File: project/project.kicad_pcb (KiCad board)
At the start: 4 copper layers, 84 x 84 mm, 163 parts, among them J101 BUS, J102 BUS, J103 FFC, J104 Back, J105 Front, J301 5V, J302 24V, J303 3V3, J401 USB_C_Receptacle_USB2.0, SW101 SW_DIP_x04, SW401 RST, SW402 MOD, U101 GX101, U102 GX101, U201 74HC595, U202 ULN2803A, U203 74HC595, U204 ULN2803A, U301 ME3121AM6G, U302 MT3406, U401 esp32-C3FH4X, U402 XL1050, U403 USBLC6-2SC6, Y401 40MHz

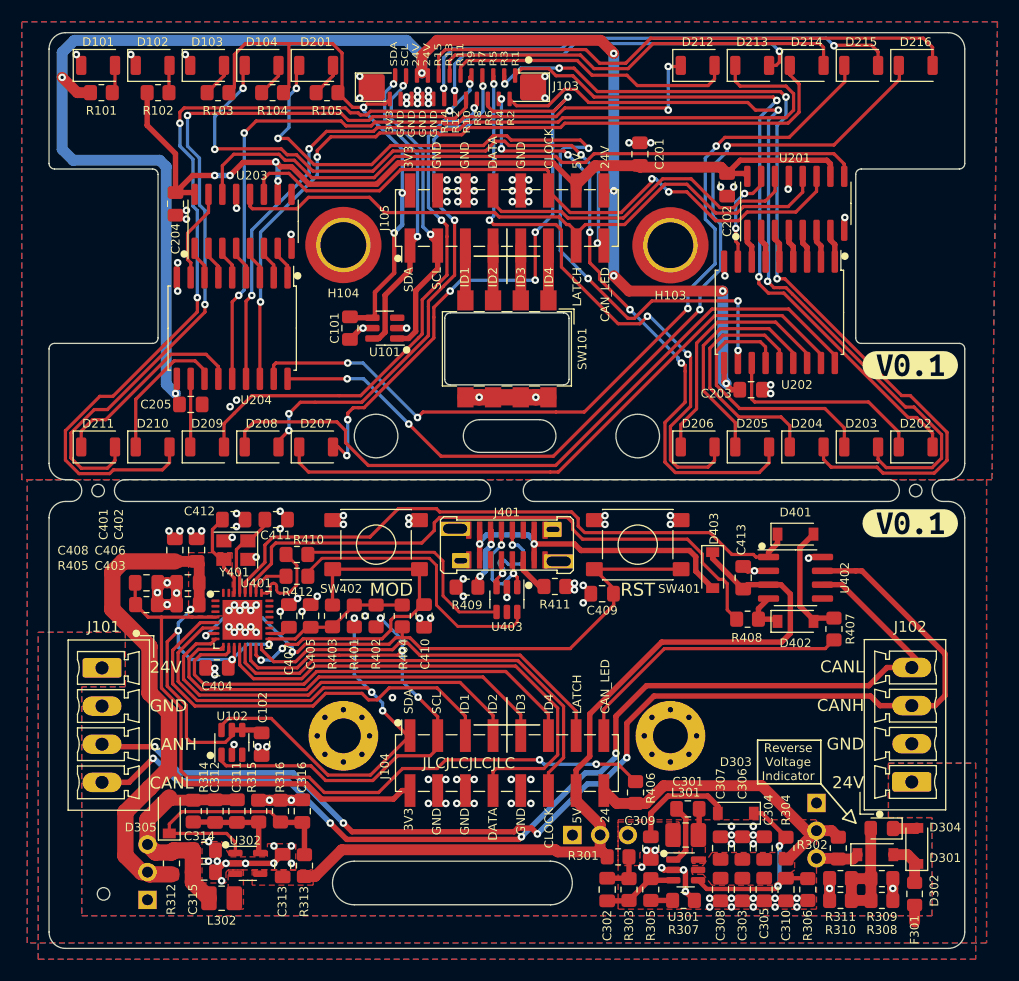
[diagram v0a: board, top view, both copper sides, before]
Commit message: adjusting hole sizes and adding qfn model
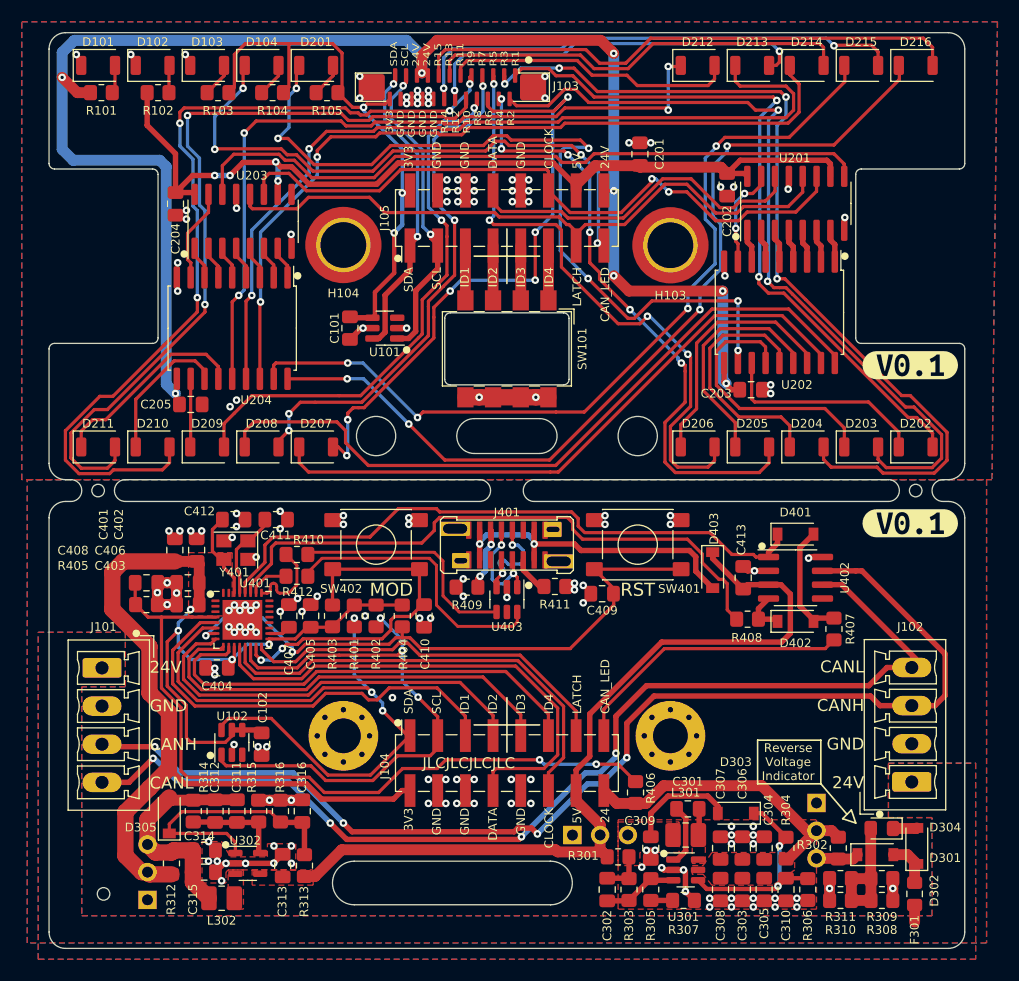
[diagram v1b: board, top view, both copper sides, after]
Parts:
- U401: footprint Package_DFN_QFN:QFN-32-1EP_5x5mm_P0.5mm_EP3.65x3.65mm -> -local:QFN-32-1EP_5x5mm_P0.5mm_EP3.65x3.65mm
- moved kibuzzard-6761E03A 0.20 mm to (168.3, 104.3)
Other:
- outline, holes or cut-outs redrawn

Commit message: few fixes and bumping up version
* reordering id bits
* moving silkscreen around
* adding hole in the center tab
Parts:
- removed kibuzzard-66DA8205: G***, kibuzzard-66DA8205
- removed kibuzzard-6750110D: G***, kibuzzard-6750110D
- removed kibuzzard-6752E14C: G***, kibuzzard-6752E14C
- removed kibuzzard-6752E284: G***, kibuzzard-6752E284
- removed kibuzzard-6752E2AC: G***, kibuzzard-6752E2AC
- removed kibuzzard-6752E2BE: G***, kibuzzard-6752E2BE
- removed kibuzzard-6752E2D3: G***, kibuzzard-6752E2D3
- removed kibuzzard-6752E2E5: G***, kibuzzard-6752E2E5
- removed kibuzzard-6752E328: G***, kibuzzard-6752E328
- removed kibuzzard-6752E335: G***, kibuzzard-6752E335
- removed kibuzzard-6752E395: G***, kibuzzard-6752E395
- removed kibuzzard-6752E39B: G***, kibuzzard-6752E39B
- removed kibuzzard-6752E3A1: G***, kibuzzard-6752E3A1
- removed kibuzzard-6752E3EF: G***, kibuzzard-6752E3EF
- removed kibuzzard-6752E3F8: G***, kibuzzard-6752E3F8
- removed kibuzzard-6752E3FE: G***, kibuzzard-6752E3FE
- removed kibuzzard-6752E405: G***, kibuzzard-6752E405
- removed kibuzzard-6752E427: G***, kibuzzard-6752E427
- removed kibuzzard-6752E433: G***, kibuzzard-6752E433
- removed kibuzzard-6752E441: G***, kibuzzard-6752E441
- removed kibuzzard-6752E448: G***, kibuzzard-6752E448
- removed kibuzzard-6752E44F: G***, kibuzzard-6752E44F
- removed kibuzzard-67570608: G***, kibuzzard-67570608
- removed kibuzzard-67570794: G***, kibuzzard-67570794
- removed kibuzzard-6757079A: G***, kibuzzard-6757079A
- removed kibuzzard-6761E03A: G***, kibuzzard-6761E03A
- removed kibuzzard-6761E048: G***, kibuzzard-6761E048
- removed kibuzzard-6761E1E4 (x2): G***, kibuzzard-6761E1E4
- added REF**: toolhole, -local:toolhole, F.Cu at (168.3, 112.5)
- added kibuzzard-679933C7: G***, kibuzzard-679933C7, F.Cu at (205.3, 101.0)
- added kibuzzard-679933D9: G***, kibuzzard-679933D9, F.Cu at (205.3, 115.5)
- added kibuzzard-67993413: G***, kibuzzard-67993413, B.Cu at (135.8, 106.5)
- added kibuzzard-67993427: G***, kibuzzard-67993427, B.Cu at (130.8, 107.0)
- added kibuzzard-67993436: G***, kibuzzard-67993436, B.Cu at (140.8, 106.5)
- added kibuzzard-67993449: G***, kibuzzard-67993449, B.Cu at (145.8, 106.5)
- added kibuzzard-67993459: G***, kibuzzard-67993459, B.Cu at (150.8, 106.5)
- added kibuzzard-679934A0: G***, kibuzzard-679934A0, B.Cu at (156.3, 104.0)
- added kibuzzard-679934B0: G***, kibuzzard-679934B0, B.Cu at (180.3, 104.0)
- added kibuzzard-679934DC: G***, kibuzzard-679934DC, B.Cu at (185.8, 106.5)
- added kibuzzard-679934EA: G***, kibuzzard-679934EA, B.Cu at (190.8, 106.5)
- added kibuzzard-67993507: G***, kibuzzard-67993507, B.Cu at (205.8, 106.5)
- added kibuzzard-67993514: G***, kibuzzard-67993514, B.Cu at (200.8, 106.5)
- added kibuzzard-67993518: G***, kibuzzard-67993518, B.Cu at (195.8, 106.5)
- added kibuzzard-6799352B: G***, kibuzzard-6799352B, B.Cu at (130.8, 75.0)
- added kibuzzard-67993537: G***, kibuzzard-67993537, B.Cu at (135.8, 75.5)
- added kibuzzard-67993543: G***, kibuzzard-67993543, B.Cu at (140.8, 75.0)
- added kibuzzard-67993570: G***, kibuzzard-67993570, B.Cu at (145.8, 75.0)
- added kibuzzard-6799357E: G***, kibuzzard-6799357E, B.Cu at (150.8, 75.0)
- added kibuzzard-67993590: G***, kibuzzard-67993590, B.Cu at (185.8, 75.0)
- added kibuzzard-6799359C: G***, kibuzzard-6799359C, B.Cu at (190.8, 75.0)
- added kibuzzard-679935A9: G***, kibuzzard-679935A9, B.Cu at (195.8, 75.0)
- added kibuzzard-679935B4: G***, kibuzzard-679935B4, B.Cu at (200.8, 75.0)
- added kibuzzard-679935C1: G***, kibuzzard-679935C1, B.Cu at (205.8, 75.0)
- added kibuzzard-679935E3: G***, kibuzzard-679935E3, B.Cu at (144.3, 151.0)
- added kibuzzard-679935F0: G***, kibuzzard-679935F0, B.Cu at (203.5, 152.2)
- added kibuzzard-6799365E: G***, kibuzzard-6799365E, B.Cu at (168.5, 122.8)
- added kibuzzard-67993A27: G***, kibuzzard-67993A27, B.Cu at (168.3, 104.4)
- moved G*** 3.61 mm to (168.5, 83.0)
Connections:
- J104 pad 11: B_ID4 -> B_ID1
- J104 pad 5: B_ID1 -> B_ID4
- J104 pad 7: B_ID2 -> B_ID3
- J104 pad 9: B_ID3 -> B_ID2
- J105 pad 11: F_ID4 -> F_ID1
- J105 pad 5: F_ID1 -> F_ID4
- J105 pad 7: F_ID2 -> F_ID3
- J105 pad 9: F_ID3 -> F_ID2
- SW101 pad 1: F_ID4 -> F_ID1
- SW101 pad 2: F_ID3 -> F_ID2
- SW101 pad 3: F_ID2 -> F_ID3
- SW101 pad 4: F_ID1 -> F_ID4
- U401 pad 10: B_ID4 -> B_ID1
- U401 pad 5: B_ID1 -> B_ID4
- U401 pad 8: B_ID2 -> B_ID3
- U401 pad 9: B_ID3 -> B_ID2
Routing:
- net B_ID4: track 42.2 -> 39.8 mm
- net B_ID1: track 39.8 -> 42.2 mm
- net B_ID3: track 40.0 -> 38.3 mm
- net B_ID2: track 38.3 -> 40.0 mm
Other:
- board text added: "SDA SCL ID4 ID3 ID2 ID1 LATCH CAN_LED"
- board text removed: "SDA SCL ID1 ID2 ID3 ID4 LATCH CAN_LED"

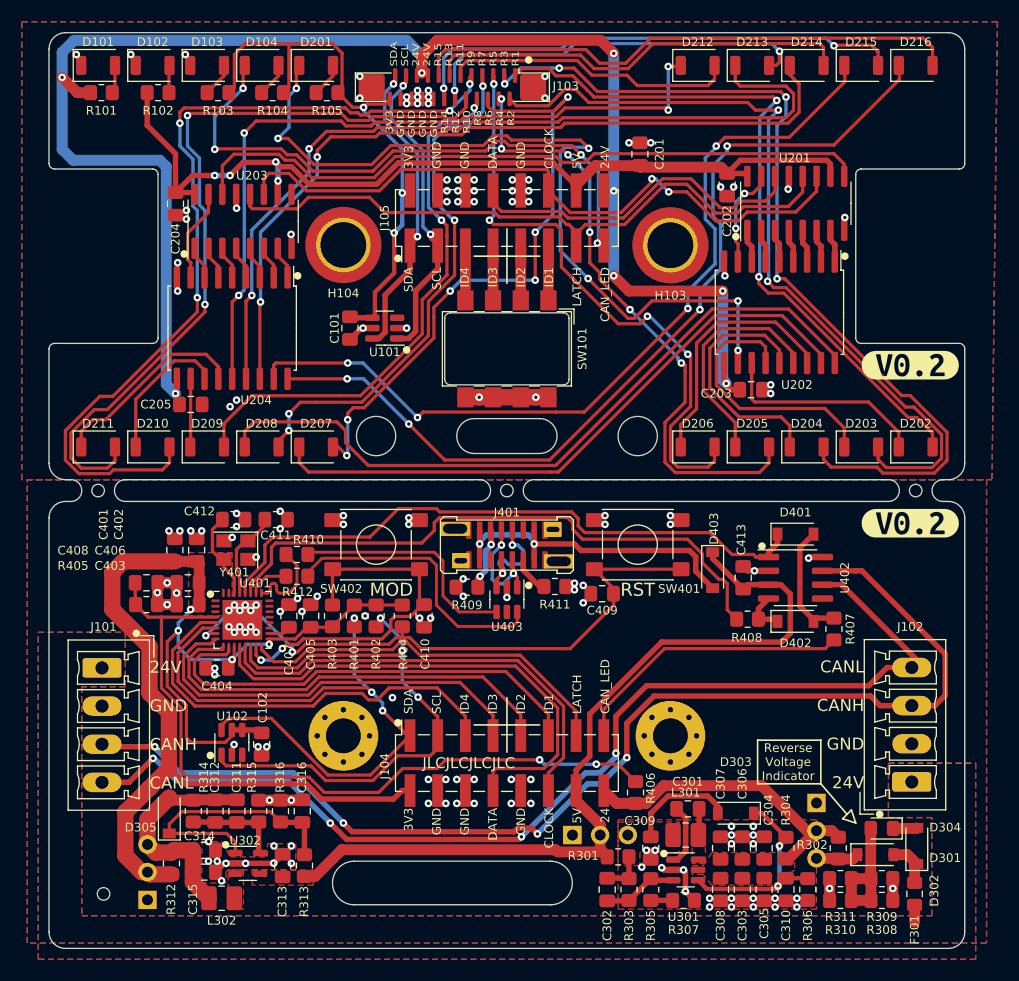
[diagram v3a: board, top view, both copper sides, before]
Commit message: improvements for next prototype
* buck makes 6v now
* using LDO for 5v with over voltage disable
* using LDO for 3v3
* adding zener to 24v led to stop it from glowing from 5v USB
* added 0.2mm heigt for USB port hole
* both buttons now 15mm height
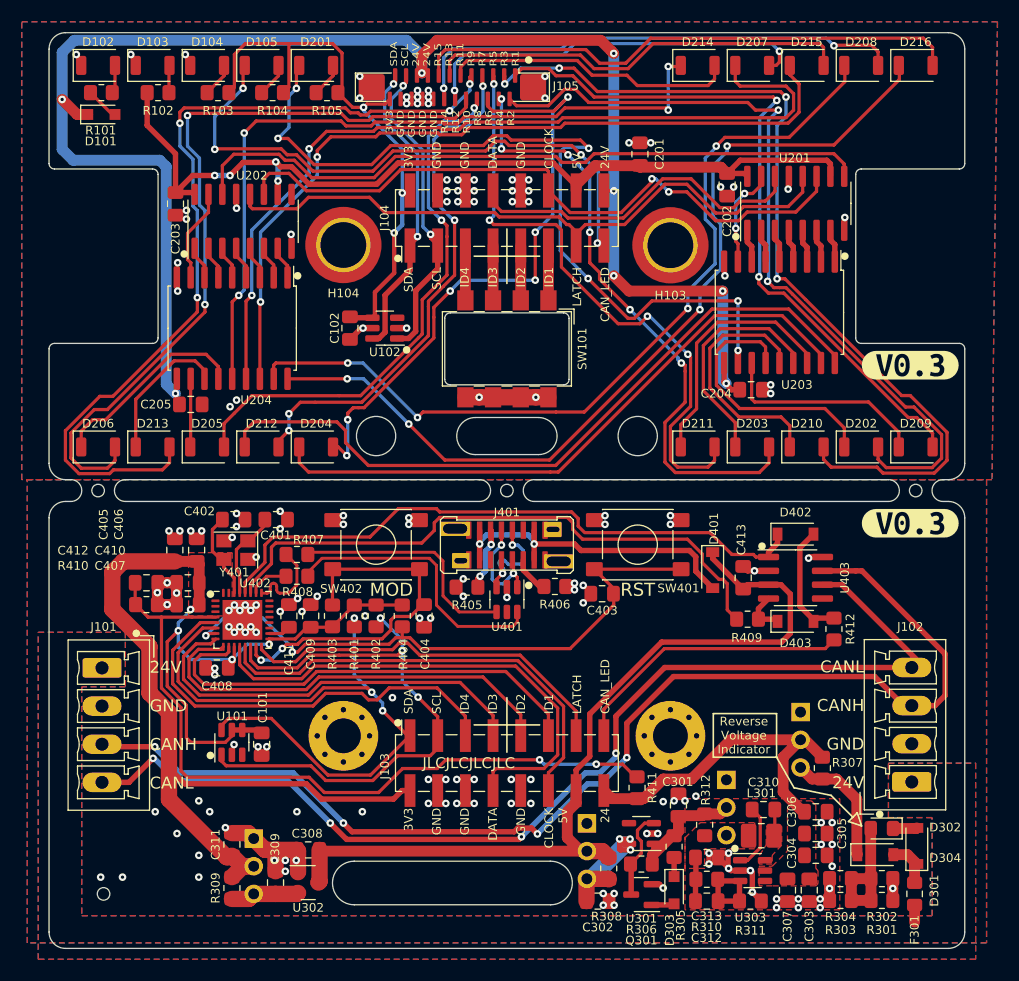
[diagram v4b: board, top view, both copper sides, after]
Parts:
- removed the C305 at (191.9, 149.1)
- removed the C310 at (193.9, 149.1)
- removed the C312 at (141.5, 141.9)
- removed C314, C315, C316: 22u/25v, Capacitor_SMD:C_0805_2012Metric_Pad1.18x1.45mm_HandSolder
- removed D305: B5819W, Diode_SMD:D_SOD-123
- removed L302: 3.3uH, Inductor_SMD:L_1008_2520Metric_Pad1.43x2.20mm_HandSolder
- removed the R304 at (193.9, 145.3)
- removed the R312 at (137.5, 146.7)
- removed R313, R314, R316: 47k, Resistor_SMD:R_0805_2012Metric_Pad1.20x1.40mm_HandSolder
- removed R315: 10k, Resistor_SMD:R_0805_2012Metric_Pad1.20x1.40mm_HandSolder
- removed kibuzzard-679933C7: G***, kibuzzard-679933C7
- removed kibuzzard-679933D9: G***, kibuzzard-679933D9
- removed kibuzzard-679935E3: G***, kibuzzard-679935E3
- removed kibuzzard-679935F0: G***, kibuzzard-679935F0
- added C301: 10u/50v, Capacitor_SMD:C_0805_2012Metric_Pad1.18x1.45mm_HandSolder, F.Cu at (184.0, 141.4)
- added C302: 22u/25v, Capacitor_SMD:C_0805_2012Metric_Pad1.18x1.45mm_HandSolder, F.Cu at (176.6, 150.2)
- added C308: 22u/25v, Capacitor_SMD:C_0805_2012Metric_Pad1.18x1.45mm_HandSolder, F.Cu at (150.0, 145.5)
- added D101: 6V8, Diode_SMD:D_SOD-323_HandSoldering, F.Cu at (131.1, 78.0)
- added J302: 5V, Connector_PinHeader_2.54mm:PinHeader_1x03_P2.54mm_Vertical, B.Cu at (175.6, 143.1)
- added Q301: MMBT3904, Package_TO_SOT_SMD:SOT-23, F.Cu at (180.6, 149.6)
- added R308: 0R1, Resistor_SMD:R_0805_2012Metric_Pad1.20x1.40mm_HandSolder, F.Cu at (177.6, 147.2)
- added R309: 0R1, Resistor_SMD:R_0805_2012Metric_Pad1.20x1.40mm_HandSolder, F.Cu at (143.0, 149.0)
- added U301: LW6550A23E, Package_TO_SOT_SMD:SOT-23-5, F.Cu at (180.6, 144.0)
- added kibuzzard-68F6C776: G***, kibuzzard-68F6C776, B.Cu at (191.0, 135.5)
- added kibuzzard-68F6C793: G***, kibuzzard-68F6C793, B.Cu at (172.0, 145.5)
- added kibuzzard-68F6C7D9: G***, kibuzzard-68F6C7D9, B.Cu at (141.0, 147.0)
- added kibuzzard-68F6C81E: G***, kibuzzard-68F6C81E, B.Cu at (134.0, 153.0)
- added kibuzzard-68F6C83B: G***, kibuzzard-68F6C83B, B.Cu at (202.0, 153.0)
- added kibuzzard-68F6C8CD: G***, kibuzzard-68F6C8CD, B.Cu at (185.0, 142.0)
- added kibuzzard-68F6C9D1: G***, kibuzzard-68F6C9D1, F.Cu at (205.3, 115.5)
- added kibuzzard-68F6C9D9: G***, kibuzzard-68F6C9D9, F.Cu at (205.3, 101.0)
- C309: value 22u/25v -> 47u/6V3
- C311: value 10p -> 47u/6V3
- C313: value 22u/25v -> 10u/50v
- D302: renamed from D304; value Reverse Vcc -> BLUE
- D303: value B5819W -> 6V8; footprint Diode_SMD:D_SOD-123 -> Diode_SMD:D_SOD-323_HandSoldering
- J304: renamed from J301; value 5V -> 6V
- R310: renamed from R303; value 150k -> 200k
- R311: renamed from R307; value 10k -> 22k
- SW401: value RST -> 15mm; footprint -local:SW_SPST_14 -> -local:SW_SPST_15
- SW402: value MOD -> 15mm
- U302: value MT3406 -> JTD6206-3.3V; footprint Package_TO_SOT_SMD:TSOT-23-5 -> Package_TO_SOT_SMD:SOT-23
- moved C313 38.9 mm to (186.6, 146.2), turned to 0 degrees
- moved C309 34.6 mm to (147.0, 148.5), turned to 90 degrees
- moved R306 15.4 mm to (180.6, 146.8), turned to 0 degrees
- moved J304 15.0 mm to (188.4, 139.1), turned to 180 degrees
- moved J303 11.3 mm to (145.0, 144.5), turned to 180 degrees
- moved C306 9.35 mm to (196.6, 142.0), turned to 0 degrees
- moved C312 9.20 mm to (186.6, 150.2), turned to 180 degrees
- moved D303 9.05 mm to (183.6, 149.2), turned to -90 degrees
- moved J301 8.46 mm to (195.2, 132.9)
- moved R312 8.46 mm to (186.4, 143.2), turned to -90 degrees
- moved R307 7.48 mm to (197.2, 138.0)
- moved R310 7.20 mm to (186.6, 148.2), turned to 180 degrees
- moved C310 6.94 mm to (191.8, 141.8)
- moved L301 6.94 mm to (191.6, 144.2)
- moved C305 6.87 mm to (196.6, 144.0), turned to 0 degrees
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- renumbered C102 to C101, C101 to C102, C204 to C203, C203 to C204, C306 to C305, C307 to C306, C308 to C307, C301 to C310, C302 to C312, C411 to C401, C412 to C402, C409 to C403, C410 to C404, C401 to C405, C402 to C406, C403 to C407, C404 to C408, C405 to C409, C406 to C410, C407 to C411, C408 to C412, D101 to D102, D102 to D103, D103 to D104, D104 to D105, D203 to D202, D205 to D203, D207 to D204, D209 to D205, D211 to D206, D213 to D207, D215 to D208, D202 to D209, D204 to D210, D206 to D211, D208 to D212, D210 to D213, D212 to D214, D214 to D215, D302 to D301, D301 to D304, D403 to D401, D401 to D402, D402 to D403, J104 to J103, J105 to J104, J103 to J105, J302 to J301, R308 to R301, R309 to R302, R310 to R303, R311 to R304, R302 to R307, R301 to R312, R409 to R405, R411 to R406, R410 to R407, R412 to R408, R408 to R409, R405 to R410, R406 to R411, R407 to R412, U102 to U101, U101 to U102, U203 to U202, U202 to U203, U301 to U303, U403 to U401, U401 to U402, U402 to U403
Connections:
- net /PSU/LX5 renamed /PSU/LX
- net Net-(D301-Pad1) renamed /PSU/VO24
- net Net-(D304-Pad2) renamed /PSU/REV_LED
- C309 pad 1: /PSU/VO5 -> /PSU/VO3
- C311 pad 1: /PSU/VO3 -> B_3V3
- C311 pad 2: /PSU/FB3 -> B_GND
- C312 pad 1: /PSU/FB5 -> /PSU/FB
- C312 pad 2: /PSU/VO5 -> /PSU/VO6
- C313 pad 1: B_5V -> /PSU/VO6
- D301 pad 1: Net-(D301-Pad2) (its old number) -> /PSU/F24
- D303 pad 1: /PSU/EN5 -> /PSU/BASE_UP
- D303 pad 2: /PSU/VO5 -> /PSU/BASE
- D304 pad 2: Net-(D301-Pad2) (its old number) -> /PSU/F24
- F301 pad 1: Net-(D301-Pad2) (its old number) -> /PSU/F24
- J304 pad 2: B_5V -> /PSU/6V
- J304 pad 3: /PSU/VO5 -> /PSU/VO6
- L301 pad 2: /PSU/VO5 -> /PSU/VO6
- R101 pad 2: F_24V -> Net-(D101-Pad2)
- R305 pad 1: /PSU/FB5 -> /PSU/BASE_UP
- R305 pad 2: Net-(R305-Pad2) -> /PSU/6V
- R306 pad 1: B_GND -> /PSU/EN
- R306 pad 2: /PSU/EN5 -> /PSU/6V
- R310 pad 1: /PSU/FB5 -> /PSU/FB
- R310 pad 2: /PSU/VO5 -> /PSU/VO6
- R311 pad 1: Net-(R305-Pad2) -> /PSU/FB
- R312 pad 1: B_5V -> /PSU/6V
- R312 pad 2: /PSU/VO5 -> /PSU/VO6
- U302 pad 1: /PSU/EN3 -> B_GND
- U302 pad 2: B_GND -> /PSU/VO3
- U302 pad 3: /PSU/LX3 -> B_5V
- U303 pad 3: /PSU/FB5 -> /PSU/FB
- U303 pad 4: /PSU/EN5 -> B_24V
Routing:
- net /PSU/EN3: track 24.4 -> 0.00 mm
- net /PSU/EN5: track 19.5 -> 0.00 mm, vias 2 -> 0
- net /PSU/VO3: track 21.0 -> 6.29 mm
- net /PSU/6V: track 0.00 -> 14.3 mm
- net /PSU/FB3: track 8.93 -> 0.00 mm
- net /PSU/EN: track 0.00 -> 8.25 mm
- net /PSU/FB: track 0.00 -> 7.98 mm
- net /PSU/VO24: track 3.94 -> 11.5 mm
- net /PSU/FB5: track 6.97 -> 0.00 mm
- net Net-(D301-Pad2) (its old number): track 4.31 -> 0.00 mm
- net /PSU/F24: track 0.00 -> 4.31 mm
- net B_GND: track 34.2 -> 38.5 mm, vias 104 -> 113
- net /PSU/VO6: track 0.00 -> 4.03 mm
- net Net-(D101-Pad2): track 0.00 -> 3.08 mm
- net B_24V: track 28.5 -> 31.3 mm
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- added copper zone on F.Cu, net /PSU/VO6
- removed copper zone on F.Cu, net /PSU/LX3
- removed copper zone on F.Cu, net /PSU/VO5
- removed copper zone on F.Cu, net B_5V
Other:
- outline, holes or cut-outs redrawn
